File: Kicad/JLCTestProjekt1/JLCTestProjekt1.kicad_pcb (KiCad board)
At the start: 2 copper layers, 43.2 x 17.8 mm, 9 parts, among them J1 Analog, J2 Digital, SW1 SW_Push

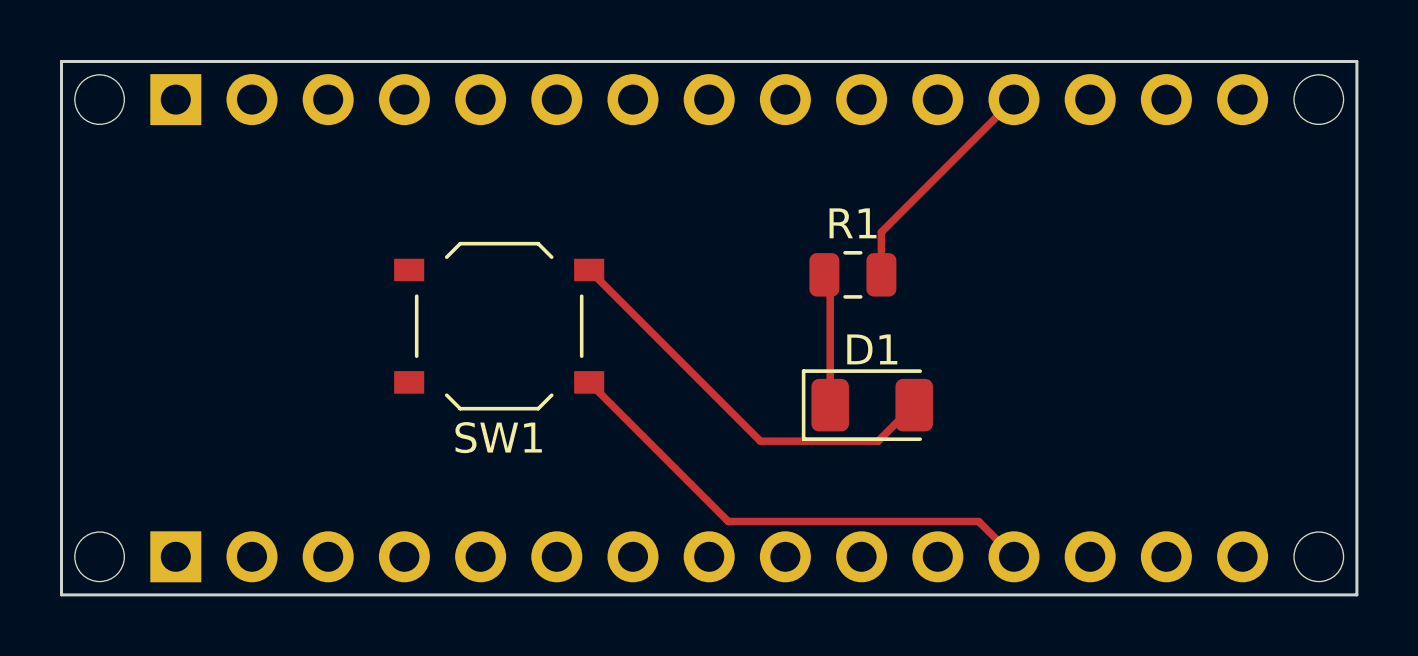
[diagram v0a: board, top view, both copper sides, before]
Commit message: Footprint korrigiert und MPN als Eigenschaft
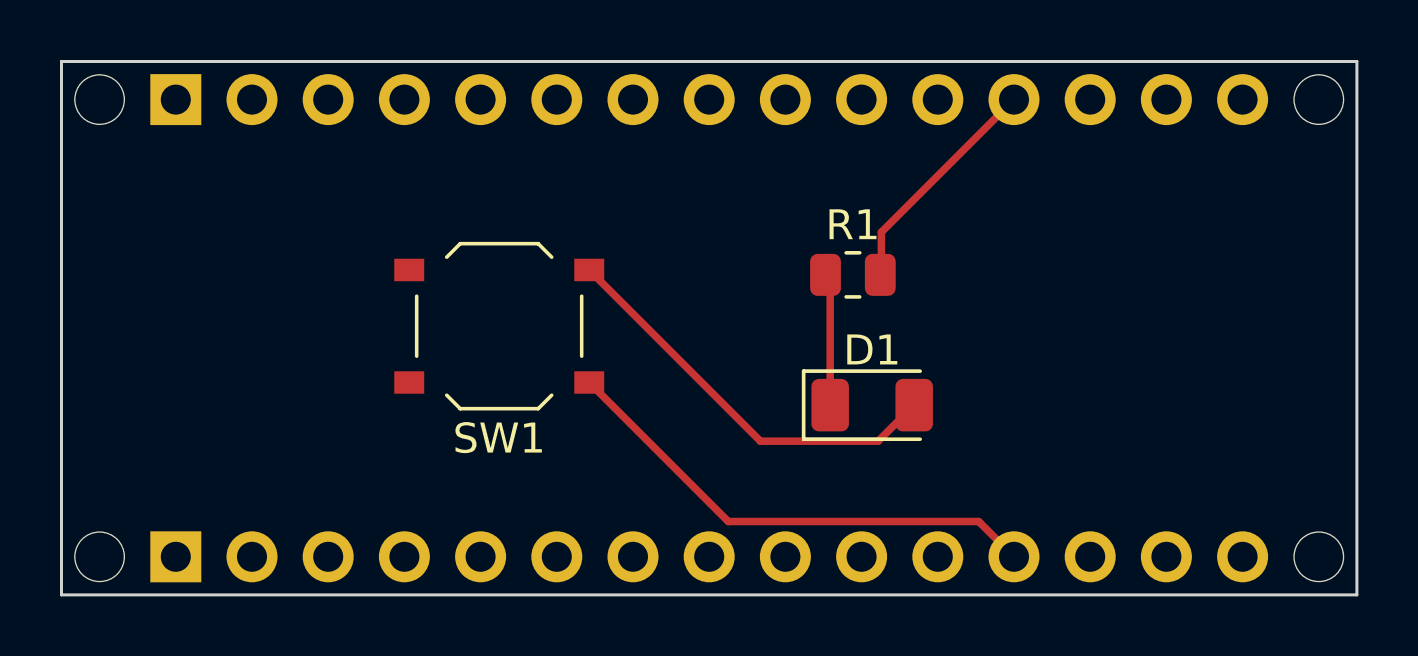
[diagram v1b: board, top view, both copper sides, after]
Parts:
- R1: footprint Capacitor_SMD:C_0805_2012Metric -> Resistor_SMD:R_0805_2012Metric
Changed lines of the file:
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@@
 		(grid_origin 100 100)
 		(pcbplotparams
-			(layerselection 0x00000000_00000000_00000000_000000a5)
+			(layerselection 0x00000000_00000000_55555555_555555f5)
 			(plot_on_all_layers_selection 0x00000000_00000000_00000000_00000000)
 			(disableapertmacros no)
@@
 			(outputformat 1)
 			(mirror no)
-			(drillshape 1)
+			(drillshape 0)
 			(scaleselection 1)
-			(outputdirectory "")
+			(outputdirectory "gerber/")
 		)
 	)
@@
 		(embedded_fonts no)
 	)
-	(footprint "Capacitor_SMD:C_0805_2012Metric"
+	(footprint "Resistor_SMD:R_0805_2012Metric"
 		(layer "F.Cu")
 		(at 126.3804 89.332)
-		(descr "Capacitor SMD 0805 (2012 Metric), square (rectangular) end terminal, IPC_7351 nominal, (Body size source: IPC-SM-782 page 76, https://www.pcb-3d.com/wordpress/wp-content/uploads/ipc-sm-782a_amendment_1_and_2.pdf, https://docs.google.com/spreadsheets/d/1BsfQQcO9C6DZCsRaXUlFlo91Tg2WpOkGARC1WS5S8t0/edit?usp=sharing), generated with kicad-footprint-generator")
-		(tags "capacitor")
+		(descr "Resistor SMD 0805 (2012 Metric), square (rectangular) end terminal, IPC_7351 nominal, (Body size source: IPC-SM-782 page 72, https://www.pcb-3d.com/wordpress/wp-content/uploads/ipc-sm-782a_amendment_1_and_2.pdf), generated with kicad-footprint-generator")
+		(tags "resistor")
 		(property "Reference" "R1"
-			(at 0 -1.68 0)
+			(at 0 -1.65 0)
 			(layer "F.SilkS")
 			(effects
@@
 		)
 		(property "Value" "150"
-			(at 0 1.68 0)
+			(at 0 1.65 0)
 			(layer "F.Fab")
 			(effects
@@
 			)
 		)
-		(property "JLCPCB" "C4256393"
+		(property "MPN" "C4256393"
 			(at 0 0 0)
 			(unlocked yes)
@@
 		(attr smd)
 		(fp_line
-			(start -0.261252 -0.735)
-			(end 0.261252 -0.735)
+			(start -0.227064 -0.735)
+			(end 0.227064 -0.735)
 			(stroke
 				(width 0.12)
@@
 		)
 		(fp_line
-			(start -0.261252 0.735)
-			(end 0.261252 0.735)
+			(start -0.227064 0.735)
+			(end 0.227064 0.735)
 			(stroke
 				(width 0.12)
@@
 		)
 		(fp_line
-			(start -1.7 -0.98)
-			(end 1.7 -0.98)
+			(start -1.68 -0.95)
+			(end 1.68 -0.95)
 			(stroke
 				(width 0.05)
@@
 		)
 		(fp_line
-			(start -1.7 0.98)
-			(end -1.7 -0.98)
+			(start -1.68 0.95)
+			(end -1.68 -0.95)
 			(stroke
 				(width 0.05)
@@
 		)
 		(fp_line
-			(start 1.7 -0.98)
-			(end 1.7 0.98)
+			(start 1.68 -0.95)
+			(end 1.68 0.95)
 			(stroke
 				(width 0.05)
@@
 		)
 		(fp_line
-			(start 1.7 0.98)
-			(end -1.7 0.98)
+			(start 1.68 0.95)
+			(end -1.68 0.95)
 			(stroke
 				(width 0.05)
@@
 		)
 		(pad "1" smd roundrect
-			(at -0.95 0)
-			(size 1 1.45)
+			(at -0.9125 0)
+			(size 1.025 1.4)
 			(layers "F.Cu" "F.Mask" "F.Paste")
-			(roundrect_rratio 0.25)
+			(roundrect_rratio 0.243902)
 			(net 25 "Net-(D1-K)")
 			(pintype "passive")
 		)
 		(pad "2" smd roundrect
-			(at 0.95 0)
-			(size 1 1.45)
+			(at 0.9125 0)
+			(size 1.025 1.4)
 			(layers "F.Cu" "F.Mask" "F.Paste")
-			(roundrect_rratio 0.25)
+			(roundrect_rratio 0.243902)
 			(net 1 "GND")
 			(pintype "passive")
 		)
 		(embedded_fonts no)
-		(model "${KICAD9_3DMODEL_DIR}/Capacitor_SMD.3dshapes/C_0805_2012Metric.wrl"
+		(model "${KICAD9_3DMODEL_DIR}/Resistor_SMD.3dshapes/R_0805_2012Metric.wrl"
 			(offset
 				(xyz 0 0 0)
@@
 			)
 		)
-		(property "JLCPCB" "C2921128"
+		(property "MPN" "C2921128"
 			(at 0 0 180)
 			(unlocked yes)
@@
 			)
 		)
-		(property "JLCPCB" "C49018"
-			(at 0 0 0)
-			(unlocked yes)
+		(property "MPN" "C49018"
+			(at 0 0 0)
+			(unlocked yes)
